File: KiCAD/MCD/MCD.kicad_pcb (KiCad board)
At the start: 2 copper layers, 208.6 x 109.7 mm, 76 parts, among them J1 DBUS_LOW, J2 DBUS_HIGH, J3 ABUS, J4 POWER, J5 JTAG, J6 Conn_01x02_Male, J7 DUART A, J8 DUART B, SW1 SW_Push, U1 XC9572XL-10VQG44C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

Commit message: abus and dbus double done
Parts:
- moved G*** 167.4 mm to (282.5, 85.5)
- moved D2 66.4 mm to (62.5, 167.5)
- moved D3 66.4 mm to (65.5, 167.5)
- moved D4 66.4 mm to (68.5, 167.5)
- moved D5 66.4 mm to (71.5, 167.5)
- moved D6 66.4 mm to (74.5, 167.5)
- moved D7 66.4 mm to (77.5, 167.5)
- moved R17 66.4 mm to (62.5, 163.0)
- moved R18 66.4 mm to (65.5, 163.0)
- moved R19 66.4 mm to (68.5, 163.0)
- moved R20 66.4 mm to (71.5, 163.0)
- moved R21 66.4 mm to (74.5, 163.0)
- moved R22 66.4 mm to (77.5, 163.0)
- moved C20 48.7 mm to (82.0, 186.5)
- moved U10 48.7 mm to (83.0, 183.0)
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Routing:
- net D15: track 145.3 -> 169.3 mm, vias 2 -> 3
- net D14: track 143.5 -> 165.9 mm, vias 2 -> 3
- net D13: track 134.5 -> 155.3 mm, vias 2 -> 3
- net D12: track 128.6 -> 147.7 mm, vias 2 -> 3
- net D11: track 126.6 -> 145.2 mm, vias 2 -> 3
- net D10: track 147.1 -> 165.3 mm, vias 2 -> 3
- net D9: track 158.6 -> 176.4 mm, vias 2 -> 3
- net D8: track 163.9 -> 181.4 mm, vias 2 -> 3
- net D7: track 145.2 -> 159.5 mm
- net D6: track 145.8 -> 159.7 mm
- net D5: track 146.0 -> 159.6 mm
- net D4: track 123.6 -> 136.8 mm
- net D3: track 139.6 -> 152.3 mm
- net D2: track 149.9 -> 160.9 mm
- net D1: track 168.9 -> 178.2 mm
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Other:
- board size 208.6 x 109.7 mm -> 197.1 x 99 mm

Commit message: updated pcb
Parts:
- moved U7 82.5 mm to (125.1, 89.0), turned to -90 degrees
- moved R23 80.9 mm to (118.6, 94.5), turned to 180 degrees
- moved C19 78.4 mm to (119.6, 91.0), turned to 90 degrees
- moved D8 76.5 mm to (115.1, 93.5), turned to -90 degrees
- moved C18 74.7 mm to (119.6, 87.0), turned to -90 degrees
- moved J7 71.4 mm to (169.5, 75.5)
- moved J8 70.9 mm to (124.5, 75.5), turned to 0 degrees
- moved R16 70.5 mm to (118.6, 83.5), turned to 180 degrees
- moved D1 67.6 mm to (115.1, 84.5), turned to 90 degrees
- moved D2 59.0 mm to (121.5, 166.1)
- moved D3 59.0 mm to (124.5, 166.0)
- moved D4 59.0 mm to (127.5, 166.0)
- moved D5 59.0 mm to (130.5, 166.0)
- moved D6 59.0 mm to (133.5, 166.0)
- moved D7 59.0 mm to (136.5, 166.0)
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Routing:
- net +5V: track 154.0 -> 86.2 mm
- net CLK: track 32.6 -> 0.00 mm
- net /SW_IN: track 10.5 -> 0.00 mm
- net RESET: track 6.68 -> 0.01 mm
- net BERR: track 6.72 -> 0.17 mm
- net TCK: track 3.67 -> 0.00 mm, vias 1 -> 0
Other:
- board size 197.1 x 99 mm -> 197 x 101.5 mm

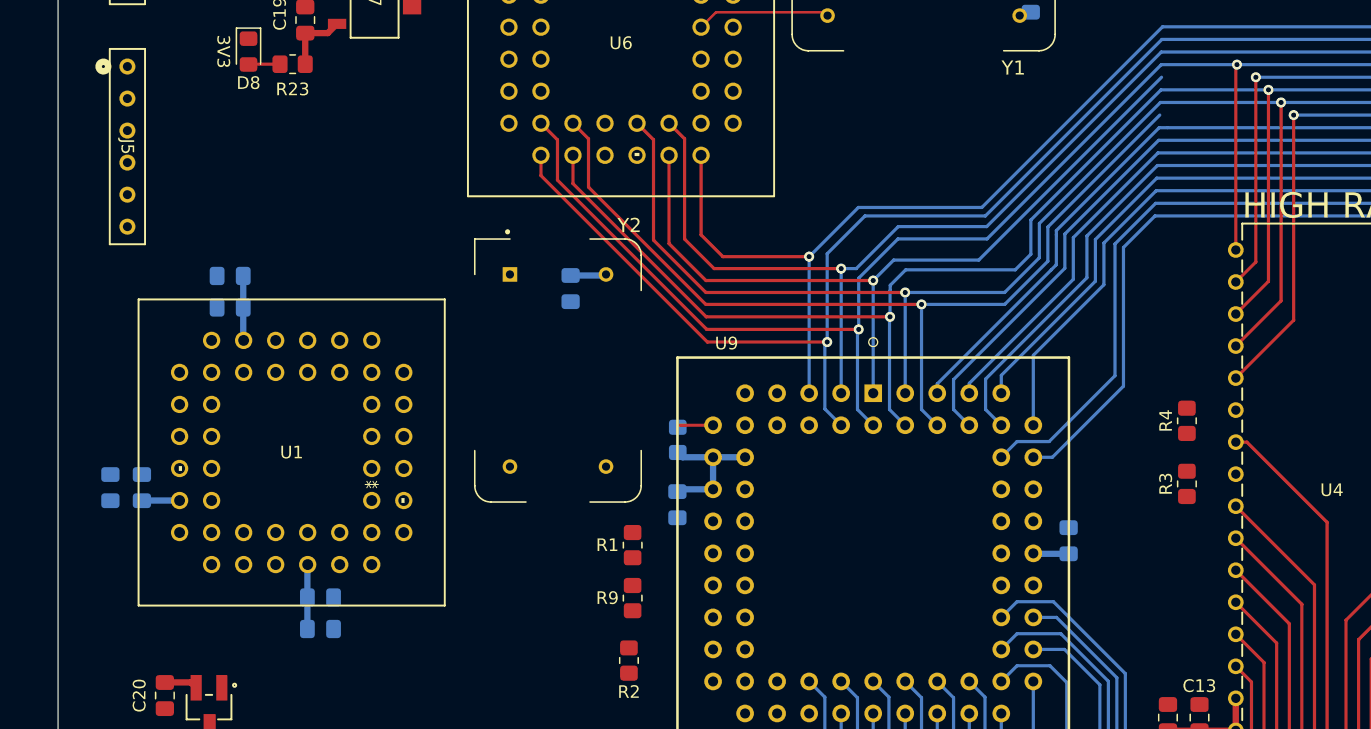
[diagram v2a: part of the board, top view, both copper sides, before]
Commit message: AHHH THE BUS WAS NOT CONNECTD THAMK YOU GF FOR POINTYING THAT ORUT
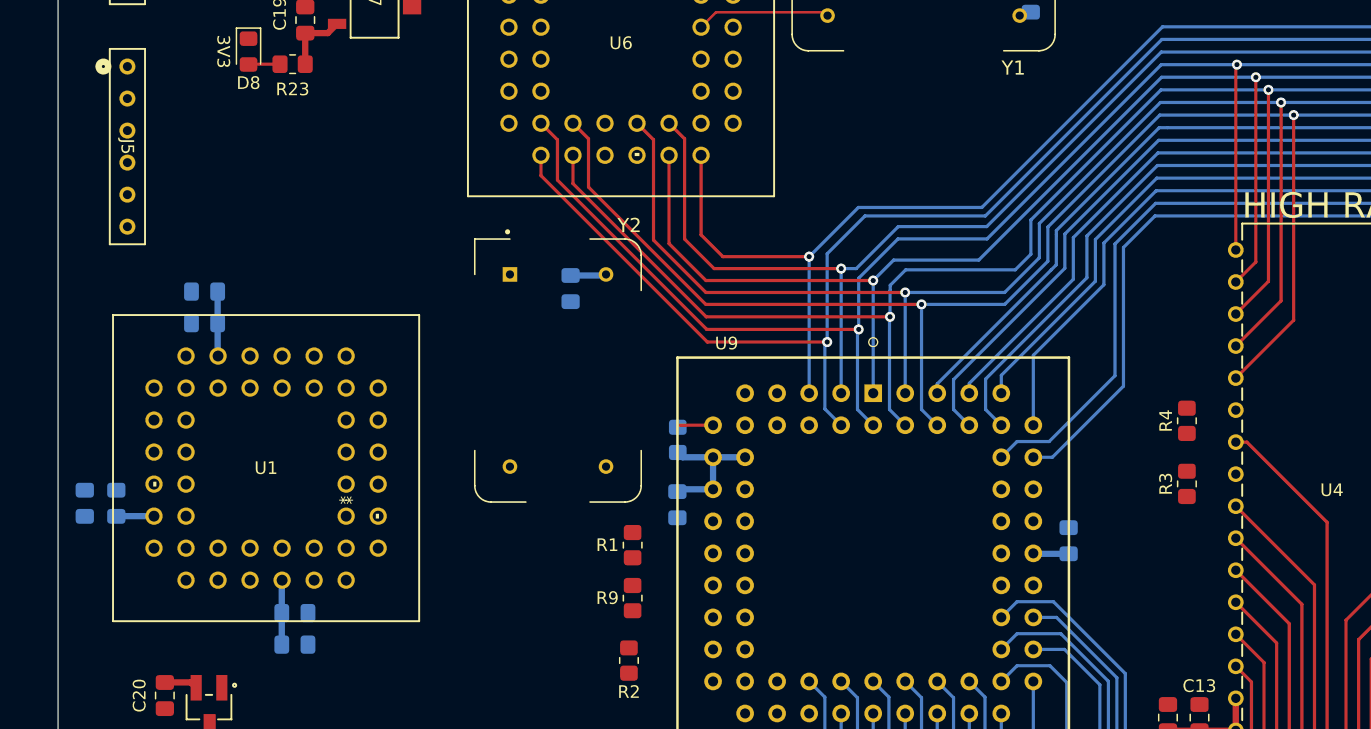
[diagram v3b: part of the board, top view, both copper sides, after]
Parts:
- moved C7 2.38 mm to (118.8, 138.0)
- moved C9 2.38 mm to (118.8, 140.5)
- moved C12 2.38 mm to (111.6, 115.0)
- moved C14 2.38 mm to (111.6, 112.5)
- moved U1 2.38 mm to (122.8, 127.8)
- moved C5 2.38 mm to (104.6, 129.3)
- moved C6 2.38 mm to (102.1, 129.3)
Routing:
- net D7: track 159.5 -> 170.1 mm
- net D4: track 136.8 -> 144.2 mm
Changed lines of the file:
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@@
   )
   (footprint "Imported:TO_11B1-RK-TP_3MM" (layer "F.Cu")
-    (at 124.88 126.53 -90)
+    (at 122.85 127.77 -90)
     (tags "8444-11B1-RK-TP ")
     (property "Datasheet_1" "https://componentsearchengine.com/Datasheets/2/XC9572XL-10VQG44C.pdf")
@@
   )
   (footprint "Capacitor_SMD:C_0805_2012Metric_Pad1.18x1.45mm_HandSolder" (layer "B.Cu")
-    (at 104.15051 128.0475 90)
+    (at 102.12051 129.2875 90)
     (descr "Capacitor SMD 0805 (2012 Metric), square (rectangular) end terminal, IPC_7351 nominal with elongated pad for handsoldering. (Body size source: IPC-SM-782 page 76, https://www.pcb-3d.com/wordpress/wp-content/uploads/ipc-sm-782a_amendment_1_and_2.pdf, https://docs.google.com/spreadsheets/d/1BsfQQcO9C6DZCsRaXUlFlo91Tg2WpOkGARC1WS5S8t0/edit?usp=sharing), generated with kicad-footprint-generator")
     (tags "capacitor handsolder")
@@
   )
   (footprint "Capacitor_SMD:C_0805_2012Metric_Pad1.18x1.45mm_HandSolder" (layer "B.Cu")
-    (at 120.81301 139.26)
+    (at 118.78301 140.5)
     (descr "Capacitor SMD 0805 (2012 Metric), square (rectangular) end terminal, IPC_7351 nominal with elongated pad for handsoldering. (Body size source: IPC-SM-782 page 76, https://www.pcb-3d.com/wordpress/wp-content/uploads/ipc-sm-782a_amendment_1_and_2.pdf, https://docs.google.com/spreadsheets/d/1BsfQQcO9C6DZCsRaXUlFlo91Tg2WpOkGARC1WS5S8t0/edit?usp=sharing), generated with kicad-footprint-generator")
     (tags "capacitor handsolder")
@@
   )
   (footprint "Capacitor_SMD:C_0805_2012Metric_Pad1.18x1.45mm_HandSolder" (layer "B.Cu")
-    (at 106.65051 128.0475 90)
+    (at 104.62051 129.2875 90)
     (descr "Capacitor SMD 0805 (2012 Metric), square (rectangular) end terminal, IPC_7351 nominal with elongated pad for handsoldering. (Body size source: IPC-SM-782 page 76, https://www.pcb-3d.com/wordpress/wp-content/uploads/ipc-sm-782a_amendment_1_and_2.pdf, https://docs.google.com/spreadsheets/d/1BsfQQcO9C6DZCsRaXUlFlo91Tg2WpOkGARC1WS5S8t0/edit?usp=sharing), generated with kicad-footprint-generator")
     (tags "capacitor handsolder")
@@
   )
   (footprint "Capacitor_SMD:C_0805_2012Metric_Pad1.18x1.45mm_HandSolder" (layer "B.Cu")
-    (at 120.81301 136.76)
+    (at 118.78301 138)
     (descr "Capacitor SMD 0805 (2012 Metric), square (rectangular) end terminal, IPC_7351 nominal with elongated pad for handsoldering. (Body size source: IPC-SM-782 page 76, https://www.pcb-3d.com/wordpress/wp-content/uploads/ipc-sm-782a_amendment_1_and_2.pdf, https://docs.google.com/spreadsheets/d/1BsfQQcO9C6DZCsRaXUlFlo91Tg2WpOkGARC1WS5S8t0/edit?usp=sharing), generated with kicad-footprint-generator")
     (tags "capacitor handsolder")
@@
   )
   (footprint "Capacitor_SMD:C_0805_2012Metric_Pad1.18x1.45mm_HandSolder" (layer "B.Cu")
-    (at 113.65051 113.76 180)
+    (at 111.62051 115 180)
     (descr "Capacitor SMD 0805 (2012 Metric), square (rectangular) end terminal, IPC_7351 nominal with elongated pad for handsoldering. (Body size source: IPC-SM-782 page 76, https://www.pcb-3d.com/wordpress/wp-content/uploads/ipc-sm-782a_amendment_1_and_2.pdf, https://docs.google.com/spreadsheets/d/1BsfQQcO9C6DZCsRaXUlFlo91Tg2WpOkGARC1WS5S8t0/edit?usp=sharing), generated with kicad-footprint-generator")
     (tags "capacitor handsolder")
@@
   )
   (footprint "Capacitor_SMD:C_0805_2012Metric_Pad1.18x1.45mm_HandSolder" (layer "B.Cu")
-    (at 113.65051 111.26 180)
+    (at 111.62051 112.5 180)
     (descr "Capacitor SMD 0805 (2012 Metric), square (rectangular) end terminal, IPC_7351 nominal with elongated pad for handsoldering. (Body size source: IPC-SM-782 page 76, https://www.pcb-3d.com/wordpress/wp-content/uploads/ipc-sm-782a_amendment_1_and_2.pdf, https://docs.google.com/spreadsheets/d/1BsfQQcO9C6DZCsRaXUlFlo91Tg2WpOkGARC1WS5S8t0/edit?usp=sharing), generated with kicad-footprint-generator")
     (tags "capacitor handsolder")
@@
   (segment (start 119.60585 92) (end 121.39415 92) (width 0.5) (layer "F.Cu") (net 3))
   (segment (start 121.39415 92) (end 122.13165 91.2625) (width 0.5) (layer "F.Cu") (net 3))
-  (segment (start 119.77551 136.76) (end 119.77551 139.26) (width 0.5) (layer "B.Cu") (net 3))
-  (segment (start 114.68801 116.33801) (end 114.72 116.37) (width 0.5) (layer "B.Cu") (net 3))
-  (segment (start 106.71051 129.07) (end 106.65051 129.01) (width 0.5) (layer "B.Cu") (net 3))
-  (segment (start 109.64 129.07) (end 106.71051 129.07) (width 0.5) (layer "B.Cu") (net 3))
-  (segment (start 114.68801 111.26) (end 114.68801 113.76) (width 0.5) (layer "B.Cu") (net 3))
-  (segment (start 119.77551 136.76) (end 119.77551 134.17449) (width 0.5) (layer "B.Cu") (net 3))
-  (segment (start 119.77551 134.17449) (end 119.8 134.15) (width 0.5) (layer "B.Cu") (net 3))
-  (segment (start 114.68801 113.76) (end 114.68801 116.33801) (width 0.5) (layer "B.Cu") (net 3))
+  (segment (start 117.74551 138) (end 117.74551 140.5) (width 0.5) (layer "B.Cu") (net 3))
+  (segment (start 112.65801 117.57801) (end 112.69 117.61) (width 0.5) (layer "B.Cu") (net 3))
+  (segment (start 104.68051 130.31) (end 104.62051 130.25) (width 0.5) (layer "B.Cu") (net 3))
+  (segment (start 107.61 130.31) (end 104.68051 130.31) (width 0.5) (layer "B.Cu") (net 3))
+  (segment (start 112.65801 112.5) (end 112.65801 115) (width 0.5) (layer "B.Cu") (net 3))
+  (segment (start 117.74551 138) (end 117.74551 135.41449) (width 0.5) (layer "B.Cu") (net 3))
+  (segment (start 117.74551 135.41449) (end 117.77 135.39) (width 0.5) (layer "B.Cu") (net 3))
+  (segment (start 112.65801 115) (end 112.65801 117.57801) (width 0.5) (layer "B.Cu") (net 3))
   (segment (start 117.60585 94.4625) (end 115.13085 94.4625) (width 0.25) (layer "F.Cu") (net 4))
   (segment (start 115.13085 94.4625) (end 115.10585 94.4875) (width 0.25) (layer "F.Cu") (net 4))
@@
   (segment (start 195 95.5) (end 222 95.5) (width 0.254) (layer "B.Cu") (net 15))
   (segment (start 173.022479 110) (end 187.522479 95.5) (width 0.254) (layer "B.Cu") (net 15))
+  (segment (start 187.522479 95.5) (end 195 95.5) (width 0.254) (layer "B.Cu") (net 15))
   (segment (start 166.273511 110) (end 173.022479 110) (width 0.254) (layer "B.Cu") (net 15))
   (segment (start 164.65051 111.623001) (end 166.273511 110) (width 0.254) (layer "B.Cu") (net 15))
@@
   (segment (start 198 98.5) (end 225 98.5) (width 0.254) (layer "B.Cu") (net 18))
   (segment (start 178.503189 107.376796) (end 187.379985 98.5) (width 0.254) (layer "B.Cu") (net 18))
+  (segment (start 187.379985 98.5) (end 198 98.5) (width 0.254) (layer "B.Cu") (net 18))
   (segment (start 235.5 99.5) (end 235.5 90.39) (width 0.254) (layer "F.Cu") (net 19))
   (segment (start 259 112.47) (end 262.89 116.36) (width 0.254) (layer "F.Cu") (net 19))

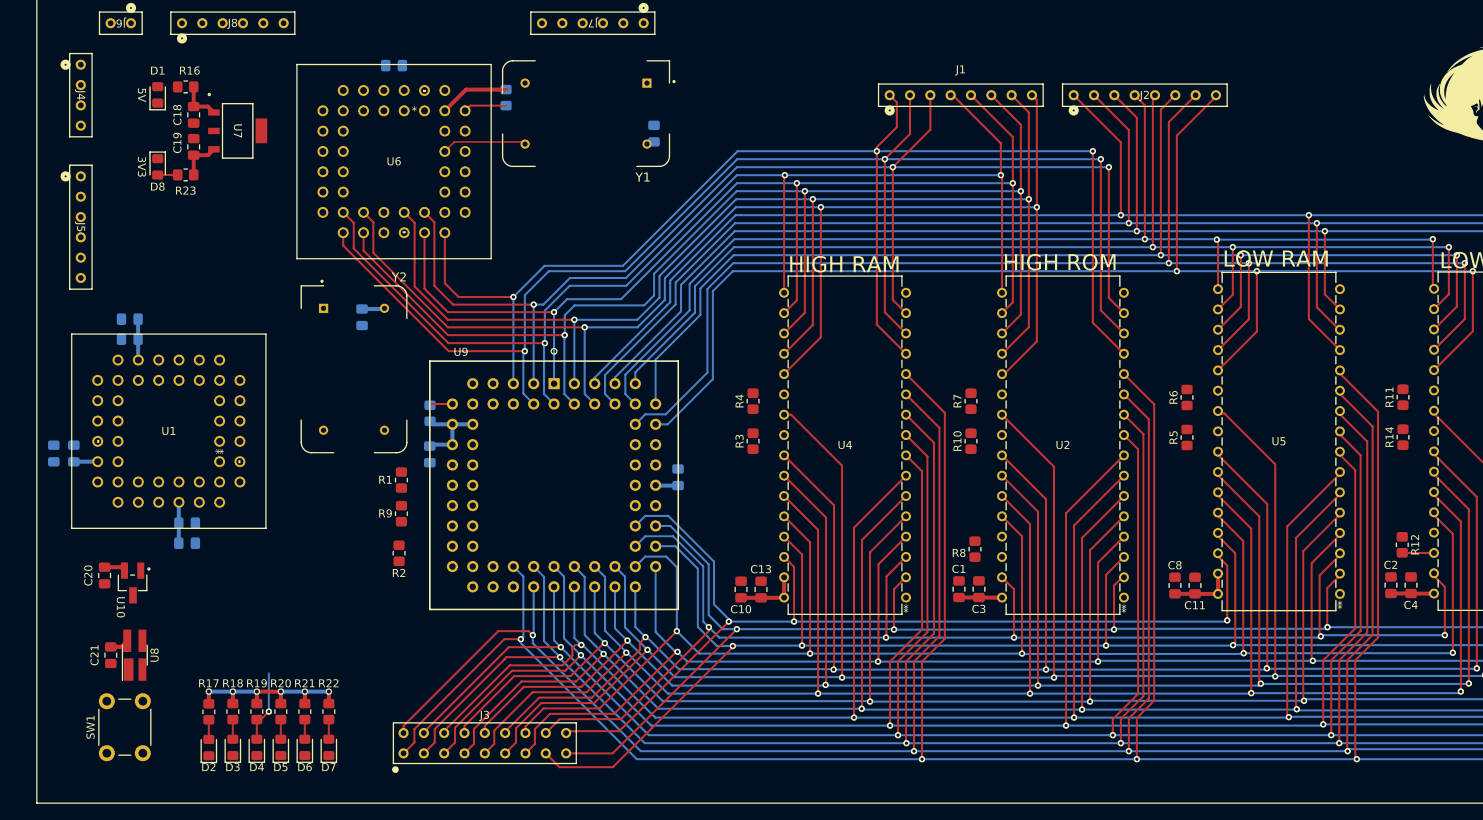
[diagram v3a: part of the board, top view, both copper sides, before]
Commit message: KICAD WAS GOOFY! anyuways decode bus is done, routing control bus
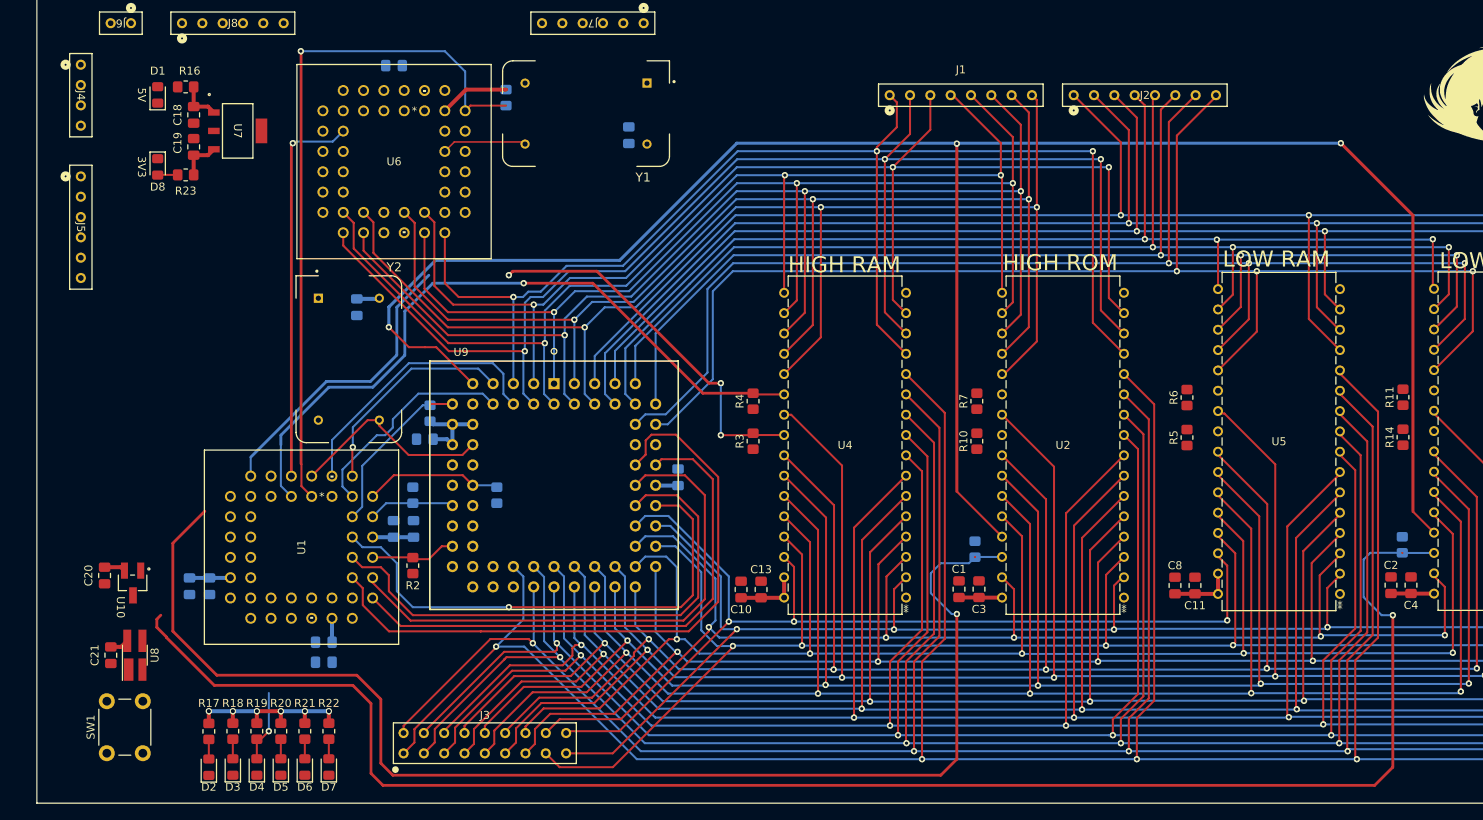
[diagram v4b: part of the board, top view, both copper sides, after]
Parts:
- R1, R12, R8, R9: moved to B.Cu
- moved C6 42.7 mm to (135.9, 155.4), turned to 180 degrees
- moved C5 39.2 mm to (135.9, 152.9), turned to 180 degrees
- moved C14 34.2 mm to (119.1, 145.9), turned to -90 degrees
- moved C12 32.4 mm to (121.6, 145.9), turned to -90 degrees
- moved C9 28.4 mm to (147.1, 138.7), turned to 90 degrees
- moved C7 25.8 mm to (144.6, 138.7), turned to 90 degrees
- moved U1 13.4 mm to (134.4, 134.7), turned to 0 degrees
- moved R1 12.1 mm to (157.5, 134.5)
- moved C15 3.16 mm to (174.0, 89.5)
- moved R9 2.72 mm to (147.0, 134.5), turned to -90 degrees
- moved R17 2.45 mm to (121.5, 164.0)
- moved D2 2.45 mm to (121.5, 168.5)
- moved D3 2.45 mm to (124.5, 168.5)
- moved D4 2.45 mm to (127.5, 168.5)
- moved D5 2.45 mm to (130.5, 168.5)
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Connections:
- U1 pad 1: CLK -> DUARTCS
- U1 pad 12: AS -> RAMHOE
- U1 pad 18: ROMLCE -> BRESET
- U1 pad 2: BERR -> DUART_DTACK
- U1 pad 20: RAMLCE -> LED0
- U1 pad 21: ROMLOE -> SRESET
- U1 pad 22: RAMLCE2 -> LED1
- U1 pad 23: RAMLOE -> LED2
- U1 pad 27: RAMHOE -> LED3
- U1 pad 28: A19 -> LED4
- U1 pad 29: A20 -> A22
- U1 pad 3: RESET -> ROMLCE
- U1 pad 30: A21 -> LED5
- U1 pad 31: A22 -> A21
- U1 pad 33: SRESET -> BERR
- U1 pad 34: BRESET -> A20
- U1 pad 36: DUART_DTACK -> A19
- U1 pad 37: LED0 -> RESET
- U1 pad 38: LED1 -> CPLD_DTACK
- U1 pad 39: LED2 -> HALT
- U1 pad 40: LED3 -> UDS
- U1 pad 41: LED4 -> LDS
- U1 pad 42: LED5 -> AS
- U1 pad 44: DUARTCS -> CLK
- U1 pad 5: HALT -> RAMLCE
- U1 pad 6: CPLD_DTACK -> ROMLOE
- U1 pad 7: UDS -> RAMLCE2
- U1 pad 8: LDS -> RAMLOE
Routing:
- net R/W: track 0.00 -> 248.4 mm, vias 0 -> 3
- net RAMHCE2: track 3.98 -> 208.0 mm, vias 0 -> 1
- net RAMLCE2: track 0.00 -> 162.4 mm, vias 0 -> 1
- net ROMLCE: track 0.00 -> 87.9 mm, vias 0 -> 1
- net ROMLOE: track 0.00 -> 84.7 mm, vias 0 -> 3
- net DUARTCS: track 5.38 -> 88.1 mm, vias 0 -> 1
- net A23: track 0.00 -> 82.1 mm
- net A22: track 0.00 -> 68.8 mm
- net A21: track 0.00 -> 68.5 mm
- net A20: track 0.00 -> 67.9 mm
- net A19: track 0.00 -> 63.7 mm, vias 0 -> 1
- net DUART_DTACK: track 0.00 -> 48.6 mm, vias 0 -> 1
- net AS: track 0.00 -> 34.8 mm
- net LDS: track 0.00 -> 27.8 mm
- net UDS: track 0.00 -> 27.5 mm, vias 0 -> 1
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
